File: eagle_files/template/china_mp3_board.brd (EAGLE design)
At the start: 27 x 45.5 mm, 10 parts

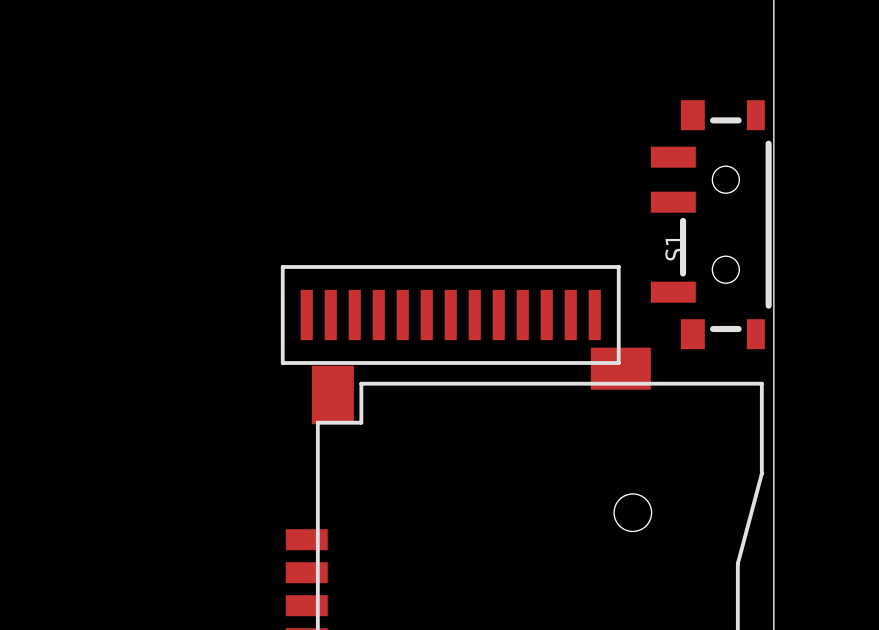
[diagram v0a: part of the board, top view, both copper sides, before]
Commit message: change lcd layer
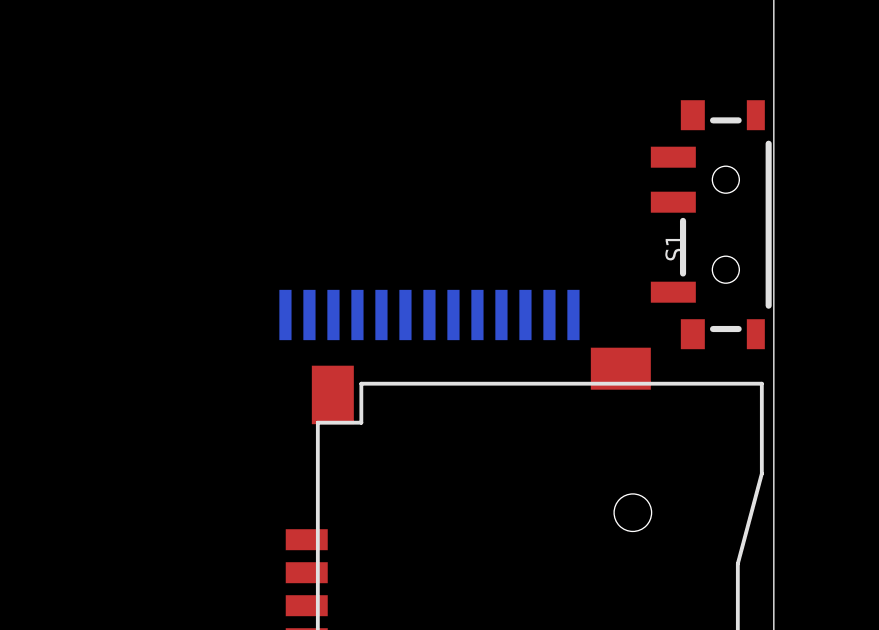
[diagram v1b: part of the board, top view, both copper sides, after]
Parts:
- moved U$7 8.89 mm to (20.3, 33.0), flipped to the bottom
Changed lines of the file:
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@@
 </element>
 <element name="SD1" library="sd-mmc" package="TF-PULL" value="TF-HOLDER" x="19.05" y="24.13" locked="yes" rot="R270"/>
-<element name="U$7" library="china_mp3_lcd" package="ONLY_PINS" value="CHINA_MP3_LCD" x="11.43" y="33.02" locked="yes"/>
+<element name="U$7" library="china_mp3_lcd" package="ONLY_PINS" value="CHINA_MP3_LCD" x="20.32" y="33.02" rot="MR0"/>
 </elements>
 <signals>
